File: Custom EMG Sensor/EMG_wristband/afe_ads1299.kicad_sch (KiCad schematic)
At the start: 1 part, among them U1 ADS1299IPAGR

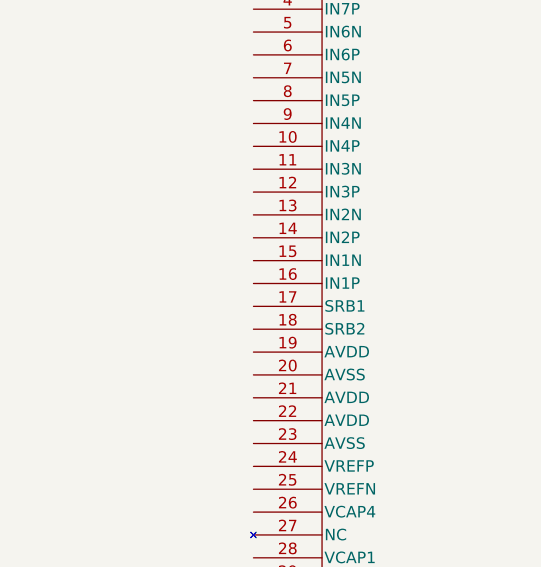
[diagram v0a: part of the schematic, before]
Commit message: Added STM32F401RET6 footprint and symbol to project and MCU sheet
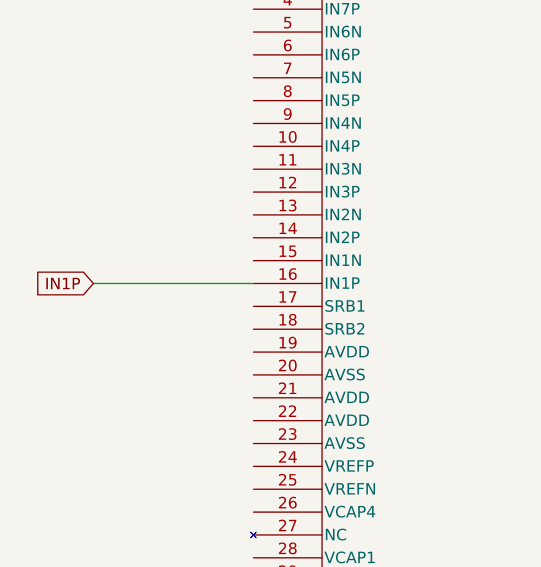
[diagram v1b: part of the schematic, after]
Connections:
- net IN1P: now reaches U1.16 (IN1P)
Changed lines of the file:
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@@
 	(generator_version "9.0")
 	(paper "A4")
+	(wire
+		(pts
+			(xy 87.63 97.79) (xy 105.41 97.79)
+		)
+		(stroke
+			(width 0)
+			(type default)
+		)
+	)
+	(global_label "IN1P"
+		(shape input)
+		(at 87.63 97.79 180)
+		(fields_autoplaced yes)
+		(effects
+			(font
+				(size 1.27 1.27)
+			)
+			(justify right)
+		)
+		(property "Intersheetrefs" "${INTERSHEET_REFS}"
+			(at 80.23 97.79 0)
+			(effects
+				(font
+					(size 1.27 1.27)
+				)
+				(justify right)
+				(hide yes)
+			)
+		)
+	)
 	(symbol
 		(lib_id "ADS1299IPAGR:ADS1299IPAGR")
